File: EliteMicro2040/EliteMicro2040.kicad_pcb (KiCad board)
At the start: 2 copper layers, 17.8 x 30.5 mm, 41 parts, among them J2 Button, U101 WL2810D33-4/TR, U2 Elite-C, U3 RP2040, Y1 2016_4P

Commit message: some small fixes regarding the silkscreen and 3d models
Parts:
- moved G*** 12.5 mm to (39.7, 41.3), turned to 180 degrees

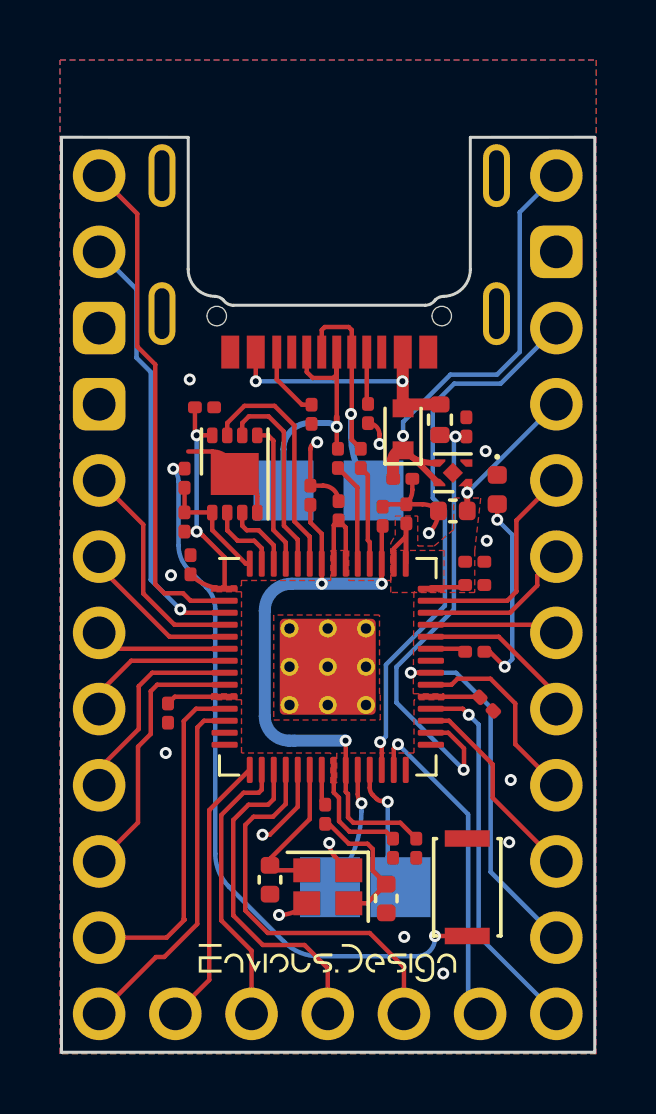
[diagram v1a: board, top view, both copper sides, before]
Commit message: swapped regulator to sot-23-3 version
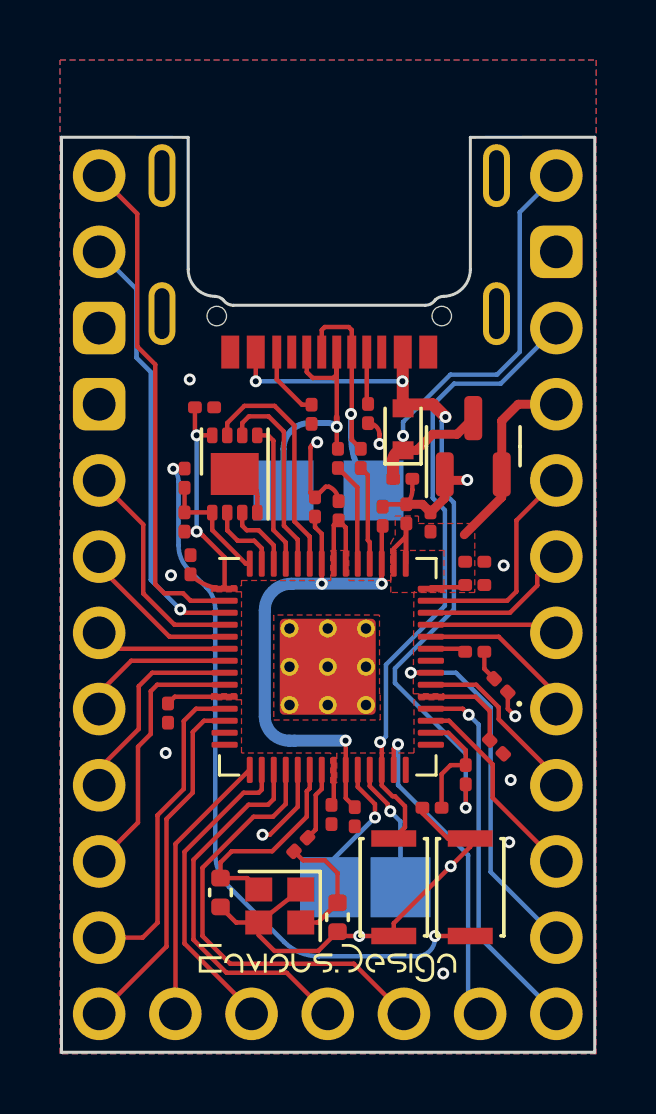
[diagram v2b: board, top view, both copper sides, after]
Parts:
- removed U101: WL2810D33-4/TR, Package_DFN_QFN:UDFN-4-1EP_1x1mm_P0.65mm_EP0.48x0.48mm
- added J1: Button, Button_Switch_SMD:SW_SPST_CK_KXT3, F.Cu at (41.9, 51.0)
- added U1: ZL6201A33S3, Package_TO_SOT_SMD:SOT-23, F.Cu at (44.5, 36.3)
- C4: value 4.7uf 0402 -> 1uf 0201; footprint Capacitor_SMD:C_0402_1005Metric -> Capacitor_SMD:C_0201_0603Metric
- D1: value Schottky Barrier SOD-723 -> SOD-523 General
- GPIO25_LED1: value LED_0402 -> LED 0201; footprint LED_SMD:LED_0402_1005Metric -> LED_SMD:LED_0201_0603Metric
- R101: value 5.6k 0402 -> 5.6k 0201; footprint Resistor_SMD:R_0402_1005Metric -> Resistor_SMD:R_0201_0603Metric
- moved R102 12.7 mm to (43.2, 48.4), turned to 180 degrees
- moved R101 11.9 mm to (44.3, 47.3), turned to 90 degrees
- moved GPIO25_LED1 6.53 mm to (45.5, 44.3), turned to 135 degrees
- moved C18 2.34 mm to (39.8, 48.6)
- moved C7 2.30 mm to (40.6, 48.7)
- moved C2 1.74 mm to (40.0, 52.0)
- moved Y1 1.72 mm to (38.1, 51.6)
- moved C19 1.70 mm to (36.1, 51.2)
- moved C11 1.47 mm to (45.3, 46.4)
- moved R7 1.30 mm to (38.8, 49.6), turned to 45 degrees
- moved C4 0.83 mm to (43.1, 38.9), turned to 90 degrees
- moved C6 0.42 mm to (39.3, 38.4)
- moved J2 0.10 mm to (44.5, 51.0)
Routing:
- net VBUS: track 11.0 -> 27.1 mm, vias 2 -> 4
- net GND: track 15.9 -> 29.7 mm, vias 15 -> 14
- net /GPIO19: track 15.7 -> 3.95 mm, vias 2 -> 0
- net Net-(GPIO25_LED1-Pad2): track 6.62 -> 1.03 mm, vias 2 -> 0
- net +1V1: track 22.0 -> 18.3 mm
- net /RUN: track 18.4 -> 21.2 mm
- net Net-(C19-Pad1): track 4.79 -> 7.06 mm
- net /GPIO15: track 13.3 -> 14.9 mm
- net /GPIO14: track 11.2 -> 12.6 mm
- net VSYS: track 17.5 -> 16.1 mm
- net Net-(R7-Pad2): track 1.04 -> 2.46 mm
- net /GPIO13: track 9.41 -> 10.4 mm
- net /SWCLK: track 4.21 -> 4.77 mm
- net /GPIO22: track 6.53 -> 5.97 mm
- net Net-(C2-Pad1): track 4.80 -> 4.24 mm
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
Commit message: swapped crystal for 3225 version
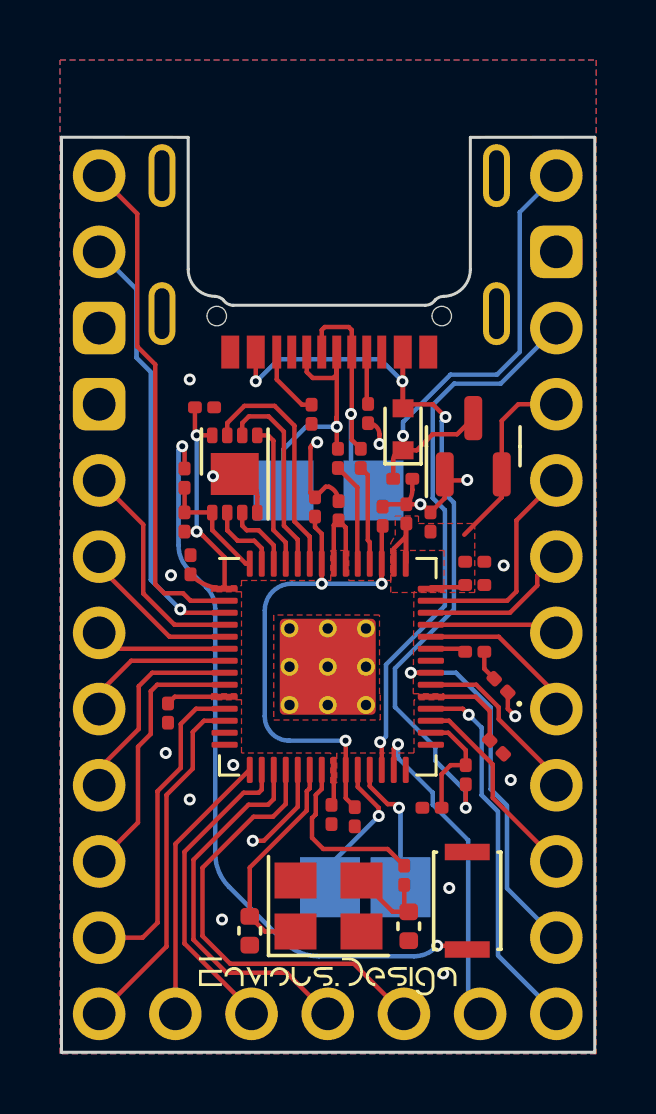
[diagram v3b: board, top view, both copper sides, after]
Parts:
- removed J1: Button, Button_Switch_SMD:SW_SPST_CK_KXT3
- Y1: value 2016_4P -> 3225-4P; footprint Crystal:Crystal_SMD_2016-4Pin_2.0x1.6mm -> Crystal:Crystal_SMD_3225-4Pin_3.2x2.5mm
- moved R7 3.60 mm to (42.2, 50.6), turned to 90 degrees
- moved C2 2.39 mm to (42.4, 52.3)
- moved Y1 1.62 mm to (39.7, 51.6), turned to 0 degrees
- moved C19 1.61 mm to (37.1, 52.5)
- moved J2 0.46 mm to (44.4, 51.5)
- moved kibuzzard-6356F424 0.45 mm to (39.7, 54.0)
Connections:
- Y1 pad 1: GND -> Net-(C19-Pad1)
- Y1 pad 2: Net-(C19-Pad1) -> GND
- Y1 pad 3: GND -> Net-(C2-Pad1)
- Y1 pad 4: Net-(C2-Pad1) -> GND
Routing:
- net GND: track 29.7 -> 14.9 mm, vias 14 -> 17
- net Net-(R7-Pad2): track 2.46 -> 5.86 mm
- net /RUN: track 21.2 -> 18.4 mm
- net Net-(C2-Pad1): track 4.24 -> 2.97 mm
- net /~{USB_BOOT}: track 24.2 -> 25.0 mm
- net VBUS: track 27.1 -> 27.8 mm
